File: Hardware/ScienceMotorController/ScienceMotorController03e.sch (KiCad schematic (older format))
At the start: 16 parts

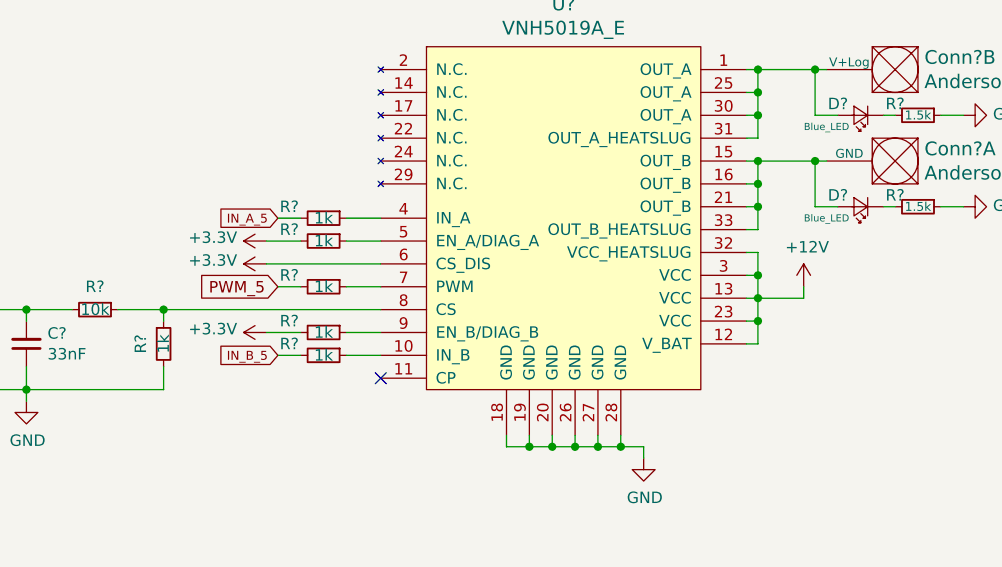
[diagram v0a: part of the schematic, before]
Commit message: changed everything to actuation, added schottky diode, added A/B flags to tiva
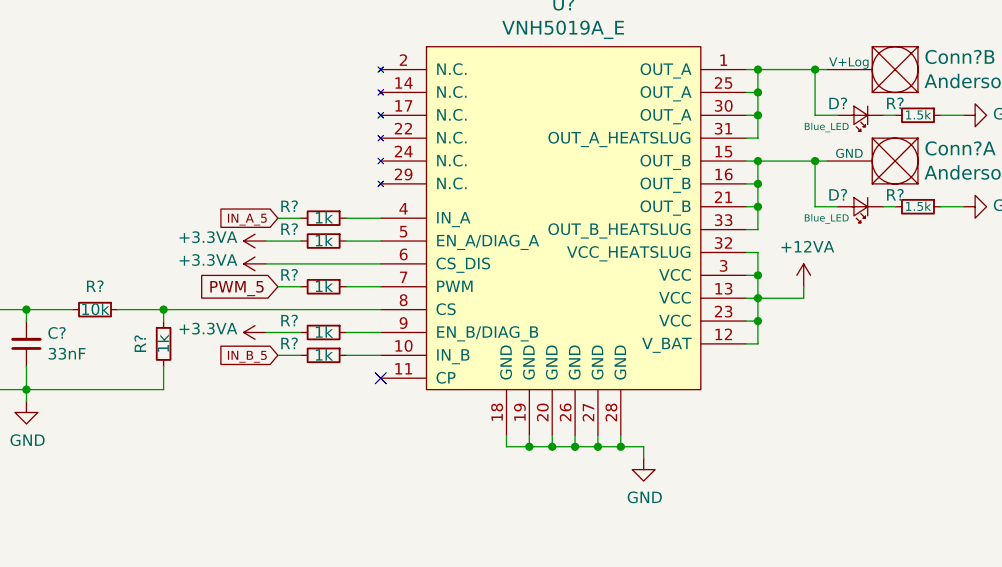
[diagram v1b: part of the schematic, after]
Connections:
- net +12V renamed +12VA
- net +3V3 renamed +3.3VA
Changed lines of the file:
@@
 	6350 4150 6350 4050
 Connection ~ 6350 4050
-$Comp
-L power:+12V #PWR?
-U 1 1 5FAB35E0
-P 6550 3900
-AR Path="/5F7D111E/5FAB35E0" Ref="#PWR?"  Part="1"
-AR Path="/5F7D111E/5FA666AF/5FAB35E0" Ref="#PWR?"  Part="1"
-F 0 "#PWR?" H 6550 3750 50  0001 C CNN
-F 1 "+12V" H 6565 4073 50  0000 C CNN
-F 2 "" H 6550 3900 50  0001 C CNN
-F 3 "" H 6550 3900 50  0001 C CNN
-	1    6550 3900
-	1    0    0    -1
-$EndComp
 Wire Wire Line
 	6550 3900 6550 3950
@@
 Wire Wire Line
 	4350 4100 4200 4100
-$Comp
-L power:+3.3V #PWR?
-U 1 1 5FAB3621
-P 4200 4100
-AR Path="/5F7D111E/5FAB3621" Ref="#PWR?"  Part="1"
-AR Path="/5F7D111E/5FA666AF/5FAB3621" Ref="#PWR?"  Part="1"
-F 0 "#PWR?" H 4200 3950 50  0001 C CNN
-F 1 "+3.3V" V 4215 4228 50  0000 L CNN
-F 2 "" H 4200 4100 50  0001 C CNN
-F 3 "" H 4200 4100 50  0001 C CNN
-	1    4200 4100
-	0    -1   -1   0
-$EndComp
-$Comp
-L power:+3.3V #PWR?
-U 1 1 5FAB3627
-P 4200 3800
-AR Path="/5F7D111E/5FAB3627" Ref="#PWR?"  Part="1"
-AR Path="/5F7D111E/5FA666AF/5FAB3627" Ref="#PWR?"  Part="1"
-F 0 "#PWR?" H 4200 3650 50  0001 C CNN
-F 1 "+3.3V" V 4215 3928 50  0000 L CNN
-F 2 "" H 4200 3800 50  0001 C CNN
-F 3 "" H 4200 3800 50  0001 C CNN
-	1    4200 3800
-	0    -1   -1   0
-$EndComp
 Wire Wire Line
 	4700 3800 4200 3800
@@
 Wire Wire Line
 	4700 3700 4550 3700
-$Comp
-L power:+3.3V #PWR?
-U 1 1 5FAB3635
-P 4200 3700
-AR Path="/5F7D111E/5FAB3635" Ref="#PWR?"  Part="1"
-AR Path="/5F7D111E/5FA666AF/5FAB3635" Ref="#PWR?"  Part="1"
-F 0 "#PWR?" H 4200 3550 50  0001 C CNN
-F 1 "+3.3V" V 4215 3828 50  0000 L CNN
-F 2 "" H 4200 3700 50  0001 C CNN
-F 3 "" H 4200 3700 50  0001 C CNN
-	1    4200 3700
-	0    -1   -1   0
-$EndComp
 Wire Wire Line
 	4350 3700 4200 3700
@@
 Text Notes 7200 6950 0    197  ~ 0
 Sheet 03e: Motor Driver 5
+$Comp
+L power:+3.3VA #PWR?
+U 1 1 5F8264AF
+P 4200 3700
+F 0 "#PWR?" H 4200 3550 50  0001 C CNN
+F 1 "+3.3VA" V 4215 3827 50  0000 L CNN
+F 2 "" H 4200 3700 50  0001 C CNN
+F 3 "" H 4200 3700 50  0001 C CNN
+	1    4200 3700
+	0    -1   -1   0
+$EndComp
+$Comp
+L power:+3.3VA #PWR?
+U 1 1 5F827713
+P 4200 3800
+F 0 "#PWR?" H 4200 3650 50  0001 C CNN
+F 1 "+3.3VA" V 4215 3927 50  0000 L CNN
+F 2 "" H 4200 3800 50  0001 C CNN
+F 3 "" H 4200 3800 50  0001 C CNN
+	1    4200 3800
+	0    -1   -1   0
+$EndComp
+$Comp
+L power:+3.3VA #PWR?
+U 1 1 5F8278A2
+P 4200 4100
+F 0 "#PWR?" H 4200 3950 50  0001 C CNN
+F 1 "+3.3VA" V 4215 4227 50  0000 L CNN
+F 2 "" H 4200 4100 50  0001 C CNN
+F 3 "" H 4200 4100 50  0001 C CNN
+	1    4200 4100
+	0    -1   -1   0
+$EndComp
+$Comp
+L power:+12VA #PWR?
+U 1 1 5F8282D6
+P 6550 3900
+F 0 "#PWR?" H 6550 3750 50  0001 C CNN
+F 1 "+12VA" H 6565 4073 50  0000 C CNN
+F 2 "" H 6550 3900 50  0001 C CNN
+F 3 "" H 6550 3900 50  0001 C CNN
+	1    6550 3900
+	1    0    0    -1
+$EndComp
 $EndSCHEMATC

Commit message: fixed hierarchical
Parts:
- added FB? (x2): Ferrite_Bead, symbol Device:Ferrite_Bead_Small
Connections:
- net at U?.1 (OUT_A), U?.25 (OUT_A), U?.30 (OUT_A)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: now also FB?.2; no longer Conn?.2 (V+Log), D?.2 (A)
- net at U?.15 (OUT_B), U?.16 (OUT_B), U?.21 (OUT_B)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: now also FB?.2; no longer Conn?.1 (GND), D?.2 (A)
- net IN_A_5 renamed In_A_5
- net IN_B_5 renamed In_B_5
- new net: Conn?.2 (V+Log), D?.2 (A), FB?.1
- new net: Conn?.1 (GND), D?.2 (A), FB?.1
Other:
- moved on the sheet: Conn?A, Conn?B, D?, R?

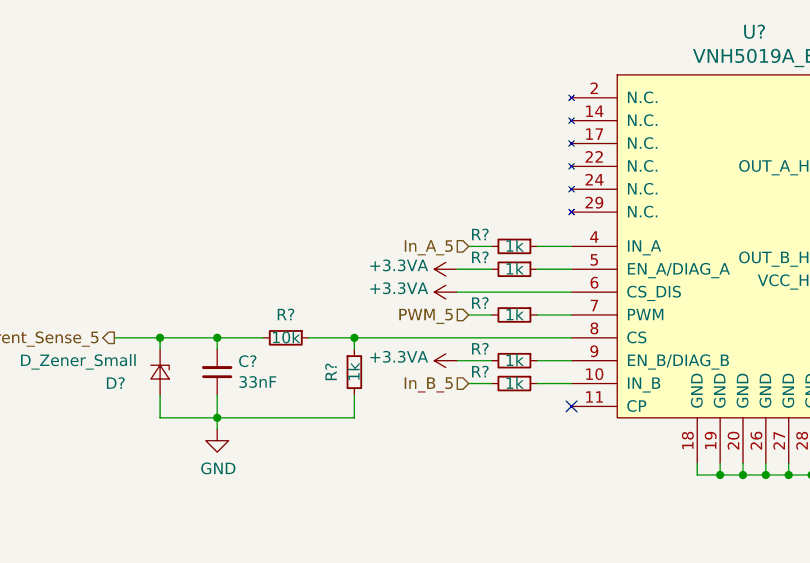
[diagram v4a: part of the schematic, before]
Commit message: Fixed 3.3V, added encoders
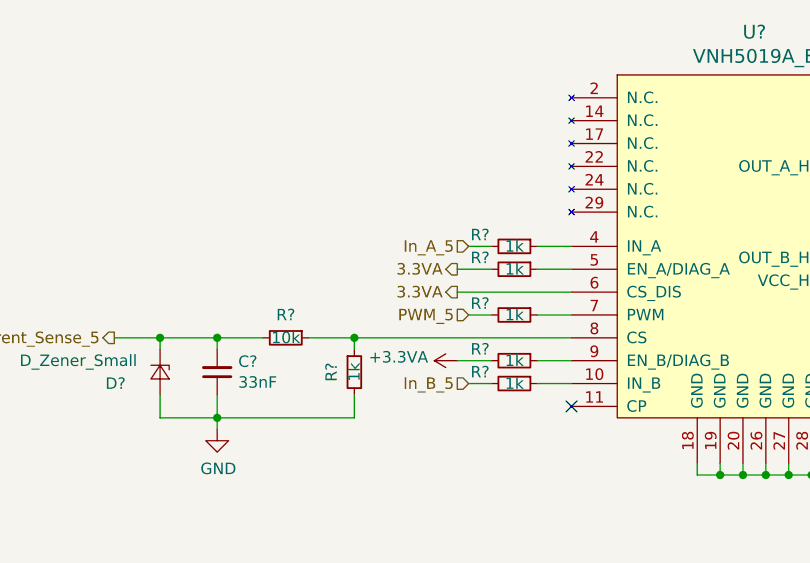
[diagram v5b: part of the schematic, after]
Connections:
- net +3.3VA: no longer R?.2, U?.6 (CS_DIS)
- new net 3.3VA: R?.2, U?.6 (CS_DIS)
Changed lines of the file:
@@
 $Descr A4 11693 8268
 encoding utf-8
-Sheet 7 10
+Sheet 7 11
 Title ""
 Date ""
@@
 $Comp
 L power:+3.3VA #PWR?
-U 1 1 5F8264AF
-P 4200 3700
-AR Path="/5F7D111E/5FA666AF/5F8264AF" Ref="#PWR?"  Part="1"
-AR Path="/5F9082FE/5F8264AF" Ref="#PWR?"  Part="1"
-AR Path="/5F7148FA/5FA34ADB/5F8264AF" Ref="#PWR?"  Part="1"
-F 0 "#PWR?" H 4200 3550 50  0001 C CNN
-F 1 "+3.3VA" V 4215 3827 50  0000 L CNN
-F 2 "" H 4200 3700 50  0001 C CNN
-F 3 "" H 4200 3700 50  0001 C CNN
-	1    4200 3700
-	0    -1   -1   0
-$EndComp
-$Comp
-L power:+3.3VA #PWR?
-U 1 1 5F827713
-P 4200 3800
-AR Path="/5F7D111E/5FA666AF/5F827713" Ref="#PWR?"  Part="1"
-AR Path="/5F9082FE/5F827713" Ref="#PWR?"  Part="1"
-AR Path="/5F7148FA/5FA34ADB/5F827713" Ref="#PWR?"  Part="1"
-F 0 "#PWR?" H 4200 3650 50  0001 C CNN
-F 1 "+3.3VA" V 4215 3927 50  0000 L CNN
-F 2 "" H 4200 3800 50  0001 C CNN
-F 3 "" H 4200 3800 50  0001 C CNN
-	1    4200 3800
-	0    -1   -1   0
-$EndComp
-$Comp
-L power:+3.3VA #PWR?
 U 1 1 5F8278A2
 P 4200 4100
@@
 Text HLabel 2700 4000 0    50   Output ~ 0
 Current_Sense_5
+Text HLabel 4200 3700 0    50   Output ~ 0
+3.3VA
+Text HLabel 4200 3800 0    50   Output ~ 0
+3.3VA
 $EndSCHEMATC

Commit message: added logic line
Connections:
- net 3.3VA is gone; now on net 3.3V: R?.2, U?.6 (CS_DIS)
- net +3.3VA renamed 3.3V
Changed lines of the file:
@@
 Sheet 03e: Motor Driver 5
-$Comp
-L power:+3.3VA #PWR?
-U 1 1 5F8278A2
-P 4200 4100
-AR Path="/5F7D111E/5FA666AF/5F8278A2" Ref="#PWR?"  Part="1"
-AR Path="/5F9082FE/5F8278A2" Ref="#PWR?"  Part="1"
-AR Path="/5F7148FA/5FA34ADB/5F8278A2" Ref="#PWR?"  Part="1"
-F 0 "#PWR?" H 4200 3950 50  0001 C CNN
-F 1 "+3.3VA" V 4215 4227 50  0000 L CNN
-F 2 "" H 4200 4100 50  0001 C CNN
-F 3 "" H 4200 4100 50  0001 C CNN
-	1    4200 4100
-	0    -1   -1   0
-$EndComp
 $Comp
 L power:+12VA #PWR?
@@
 Current_Sense_5
 Text HLabel 4200 3700 0    50   Output ~ 0
-3.3VA
+3.3V
 Text HLabel 4200 3800 0    50   Output ~ 0
-3.3VA
+3.3V
+Text HLabel 4200 4100 0    50   Output ~ 0
+3.3V
 $EndSCHEMATC

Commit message: annotated
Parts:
- C6: renamed from C?; footprint (none) -> Capacitor_SMD:C_0603_1608Metric_Pad1.05x0.95mm_HandSolder
- gave numbers to parts that had none: 16
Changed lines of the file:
@@
 AR Path="/5F7D111E/5FA666AF/5FAB35CE" Ref="U?"  Part="1"
 AR Path="/5F9082FE/5FAB35CE" Ref="U?"  Part="1"
-AR Path="/5F7148FA/5FA34ADB/5FAB35CE" Ref="U?"  Part="1"
-F 0 "U?" H 5500 6037 60  0000 C CNN
+AR Path="/5F7148FA/5FA34ADB/5FAB35CE" Ref="U6"  Part="1"
+F 0 "U6" H 5500 6037 60  0000 C CNN
 F 1 "VNH5019A_E" H 5500 5931 60  0000 C CNN
 F 2 "" H 4900 5650 60  0001 C CNN
@@
 AR Path="/5F7D111E/5FA666AF/5FAB35EB" Ref="R?"  Part="1"
 AR Path="/5F9082FE/5FAB35EB" Ref="R?"  Part="1"
-AR Path="/5F7148FA/5FA34ADB/5FAB35EB" Ref="R?"  Part="1"
-F 0 "R?" V 4400 3750 50  0000 C CNN
+AR Path="/5F7148FA/5FA34ADB/5FAB35EB" Ref="R37"  Part="1"
+F 0 "R37" V 4400 3750 50  0000 C CNN
 F 1 "1k" V 4450 3900 50  0000 C CNN
 F 2 "" H 4450 3900 50  0001 C CNN
@@
 AR Path="/5F7D111E/5FA666AF/5FAB35F1" Ref="R?"  Part="1"
 AR Path="/5F9082FE/5FAB35F1" Ref="R?"  Part="1"
-AR Path="/5F7148FA/5FA34ADB/5FAB35F1" Ref="R?"  Part="1"
-F 0 "R?" V 3650 4150 50  0000 C CNN
+AR Path="/5F7148FA/5FA34ADB/5FAB35F1" Ref="R34"  Part="1"
+F 0 "R34" V 3650 4150 50  0000 C CNN
 F 1 "1k" V 3750 4150 50  0000 C CNN
 F 2 "" H 3750 4150 50  0001 C CNN
@@
 AR Path="/5F7D111E/5FA666AF/5FAB35F7" Ref="C?"  Part="1"
 AR Path="/5F9082FE/5FAB35F7" Ref="C?"  Part="1"
-AR Path="/5F7148FA/5FA34ADB/5FAB35F7" Ref="C?"  Part="1"
-F 0 "C?" H 3058 4104 50  0000 R CNN
+AR Path="/5F7148FA/5FA34ADB/5FAB35F7" Ref="C6"  Part="1"
+F 0 "C6" H 3058 4104 50  0000 R CNN
 F 1 "33nF" H 3058 4195 50  0000 R CNN
-F 2 "" H 3150 4150 50  0001 C CNN
+F 2 "Capacitor_SMD:C_0603_1608Metric_Pad1.05x0.95mm_HandSolder" H 3150 4150 50  0001 C CNN
 F 3 "~" H 3150 4150 50  0001 C CNN
 	1    3150 4150
@@
 AR Path="/5F7D111E/5FA666AF/5FAB35FD" Ref="D?"  Part="1"
 AR Path="/5F9082FE/5FAB35FD" Ref="D?"  Part="1"
-AR Path="/5F7148FA/5FA34ADB/5FAB35FD" Ref="D?"  Part="1"
-F 0 "D?" V 2950 4000 50  0000 R CNN
+AR Path="/5F7148FA/5FA34ADB/5FAB35FD" Ref="D16"  Part="1"
+F 0 "D16" V 2950 4000 50  0000 R CNN
 F 1 "D_Zener_Small" V 2850 4050 50  0000 R CNN
 F 2 "" V 2900 4150 50  0001 C CNN
@@
 AR Path="/5F7D111E/5FA666AF/5FAB3603" Ref="R?"  Part="1"
 AR Path="/5F9082FE/5FAB3603" Ref="R?"  Part="1"
-AR Path="/5F7148FA/5FA34ADB/5FAB3603" Ref="R?"  Part="1"
-F 0 "R?" V 3350 4000 50  0000 C CNN
+AR Path="/5F7148FA/5FA34ADB/5FAB3603" Ref="R33"  Part="1"
+F 0 "R33" V 3350 4000 50  0000 C CNN
 F 1 "10k" V 3450 4000 50  0000 C CNN
 F 2 "" H 3450 4000 50  0001 C CNN
@@
 AR Path="/5F7D111E/5FA666AF/5FAB3619" Ref="R?"  Part="1"
 AR Path="/5F9082FE/5FAB3619" Ref="R?"  Part="1"
-AR Path="/5F7148FA/5FA34ADB/5FAB3619" Ref="R?"  Part="1"
-F 0 "R?" V 4400 3950 50  0000 C CNN
+AR Path="/5F7148FA/5FA34ADB/5FAB3619" Ref="R38"  Part="1"
+F 0 "R38" V 4400 3950 50  0000 C CNN
 F 1 "1k" V 4450 4100 50  0000 C CNN
 F 2 "" H 4450 4100 50  0001 C CNN
@@
 AR Path="/5F7D111E/5FA666AF/5FAB362E" Ref="R?"  Part="1"
 AR Path="/5F9082FE/5FAB362E" Ref="R?"  Part="1"
-AR Path="/5F7148FA/5FA34ADB/5FAB362E" Ref="R?"  Part="1"
-F 0 "R?" V 4400 3550 50  0000 C CNN
+AR Path="/5F7148FA/5FA34ADB/5FAB362E" Ref="R36"  Part="1"
+F 0 "R36" V 4400 3550 50  0000 C CNN
 F 1 "1k" V 4450 3700 50  0000 C CNN
 F 2 "" H 4450 3700 50  0001 C CNN
@@
 AR Path="/5F7D111E/5FA666AF/5FAB363C" Ref="R?"  Part="1"
 AR Path="/5F9082FE/5FAB363C" Ref="R?"  Part="1"
-AR Path="/5F7148FA/5FA34ADB/5FAB363C" Ref="R?"  Part="1"
-F 0 "R?" V 4400 3450 50  0000 C CNN
+AR Path="/5F7148FA/5FA34ADB/5FAB363C" Ref="R35"  Part="1"
+F 0 "R35" V 4400 3450 50  0000 C CNN
 F 1 "1k" V 4450 3600 50  0000 C CNN
 F 2 "" H 4450 3600 50  0001 C CNN
@@
 AR Path="/5F7D111E/5FA666AF/5FAB3646" Ref="R?"  Part="1"
 AR Path="/5F9082FE/5FAB3646" Ref="R?"  Part="1"
-AR Path="/5F7148FA/5FA34ADB/5FAB3646" Ref="R?"  Part="1"
-F 0 "R?" V 4400 4050 50  0000 C CNN
+AR Path="/5F7148FA/5FA34ADB/5FAB3646" Ref="R39"  Part="1"
+F 0 "R39" V 4400 4050 50  0000 C CNN
 F 1 "1k" V 4450 4200 50  0000 C CNN
 F 2 "" H 4450 4200 50  0001 C CNN
@@
 AR Path="/5F7D111E/5FA666AF/5FAB365E" Ref="#PWR?"  Part="1"
 AR Path="/5F9082FE/5FAB365E" Ref="#PWR?"  Part="1"
-AR Path="/5F7148FA/5FA34ADB/5FAB365E" Ref="#PWR?"  Part="1"
-F 0 "#PWR?" H 5850 4400 50  0001 C CNN
+AR Path="/5F7148FA/5FA34ADB/5FAB365E" Ref="#PWR032"  Part="1"
+F 0 "#PWR032" H 5850 4400 50  0001 C CNN
 F 1 "GND" H 5855 4477 50  0000 C CNN
 F 2 "" H 5850 4650 50  0001 C CNN
@@
 AR Path="/5F7D111E/5FA666AF/5FAB3668" Ref="#PWR?"  Part="1"
 AR Path="/5F9082FE/5FAB3668" Ref="#PWR?"  Part="1"
-AR Path="/5F7148FA/5FA34ADB/5FAB3668" Ref="#PWR?"  Part="1"
-F 0 "#PWR?" H 3150 4150 50  0001 C CNN
+AR Path="/5F7148FA/5FA34ADB/5FAB3668" Ref="#PWR031"  Part="1"
+F 0 "#PWR031" H 3150 4150 50  0001 C CNN
 F 1 "GND" H 3155 4227 50  0000 C CNN
 F 2 "" H 3150 4400 50  0001 C CNN
@@
 AR Path="/5F7D111E/5FA666AF/5FAB3680" Ref="Conn?"  Part="1"
 AR Path="/5F9082FE/5FAB3680" Ref="Conn?"  Part="1"
-AR Path="/5F7148FA/5FA34ADB/5FAB3680" Ref="Conn?"  Part="1"
-F 0 "Conn?" H 7472 3297 60  0000 R CNN
+AR Path="/5F7148FA/5FA34ADB/5FAB3680" Ref="Conn5"  Part="1"
+F 0 "Conn5" H 7472 3297 60  0000 R CNN
 F 1 "AndersonPP" H 7472 3403 60  0000 R CNN
 F 2 "" H 7350 2700 60  0001 C CNN
@@
 AR Path="/5F7D111E/5FA666AF/5FAB3686" Ref="Conn?"  Part="2"
 AR Path="/5F9082FE/5FAB3686" Ref="Conn?"  Part="2"
-AR Path="/5F7148FA/5FA34ADB/5FAB3686" Ref="Conn?"  Part="2"
-F 0 "Conn?" H 7472 2897 60  0000 R CNN
+AR Path="/5F7148FA/5FA34ADB/5FAB3686" Ref="Conn5"  Part="2"
+F 0 "Conn5" H 7472 2897 60  0000 R CNN
 F 1 "AndersonPP" H 7472 3003 60  0000 R CNN
 F 2 "" H 7350 2300 60  0001 C CNN
@@
 AR Path="/5F7D111E/5FA666AF/5FAB369A" Ref="D?"  Part="1"
 AR Path="/5F9082FE/5FAB369A" Ref="D?"  Part="1"
-AR Path="/5F7148FA/5FA34ADB/5FAB369A" Ref="D?"  Part="1"
-F 0 "D?" H 7350 3100 50  0000 C CNN
+AR Path="/5F7148FA/5FA34ADB/5FAB369A" Ref="D17"  Part="1"
+F 0 "D17" H 7350 3100 50  0000 C CNN
 F 1 "Blue_LED" H 7400 3200 31  0000 C CNN
 F 2 "" V 7250 3150 50  0001 C CNN
@@
 AR Path="/5F7D111E/5FA666AF/5FAB36A0" Ref="D?"  Part="1"
 AR Path="/5F9082FE/5FAB36A0" Ref="D?"  Part="1"
-AR Path="/5F7148FA/5FA34ADB/5FAB36A0" Ref="D?"  Part="1"
-F 0 "D?" H 7350 3500 50  0000 C CNN
+AR Path="/5F7148FA/5FA34ADB/5FAB36A0" Ref="D18"  Part="1"
+F 0 "D18" H 7350 3500 50  0000 C CNN
 F 1 "Blue_LED" H 7400 3600 31  0000 C CNN
 F 2 "" V 7250 3550 50  0001 C CNN
@@
 AR Path="/5F7D111E/5FA666AF/5FAB36A6" Ref="R?"  Part="1"
 AR Path="/5F9082FE/5FAB36A6" Ref="R?"  Part="1"
-AR Path="/5F7148FA/5FA34ADB/5FAB36A6" Ref="R?"  Part="1"
-F 0 "R?" V 7450 3450 50  0000 C CNN
+AR Path="/5F7148FA/5FA34ADB/5FAB36A6" Ref="R41"  Part="1"
+F 0 "R41" V 7450 3450 50  0000 C CNN
 F 1 "1.5k" V 7500 3550 39  0000 C CNN
 F 2 "" H 7500 3550 50  0001 C CNN
@@
 AR Path="/5F7D111E/5FA666AF/5FAB36AC" Ref="R?"  Part="1"
 AR Path="/5F9082FE/5FAB36AC" Ref="R?"  Part="1"
-AR Path="/5F7148FA/5FA34ADB/5FAB36AC" Ref="R?"  Part="1"
-F 0 "R?" V 7450 3050 50  0000 C CNN
+AR Path="/5F7148FA/5FA34ADB/5FAB36AC" Ref="R40"  Part="1"
+F 0 "R40" V 7450 3050 50  0000 C CNN
 F 1 "1.5k" V 7500 3150 39  0000 C CNN
 F 2 "" H 7500 3150 50  0001 C CNN
@@
 AR Path="/5F7D111E/5FA666AF/5FAB36B4" Ref="#PWR?"  Part="1"
 AR Path="/5F9082FE/5FAB36B4" Ref="#PWR?"  Part="1"
-AR Path="/5F7148FA/5FA34ADB/5FAB36B4" Ref="#PWR?"  Part="1"
-F 0 "#PWR?" H 7700 2900 50  0001 C CNN
+AR Path="/5F7148FA/5FA34ADB/5FAB36B4" Ref="#PWR034"  Part="1"
+F 0 "#PWR034" H 7700 2900 50  0001 C CNN
 F 1 "GND" V 7705 3022 50  0000 R CNN
 F 2 "" H 7700 3150 50  0001 C CNN
@@
 AR Path="/5F7D111E/5FA666AF/5FAB36BA" Ref="#PWR?"  Part="1"
 AR Path="/5F9082FE/5FAB36BA" Ref="#PWR?"  Part="1"
-AR Path="/5F7148FA/5FA34ADB/5FAB36BA" Ref="#PWR?"  Part="1"
-F 0 "#PWR?" H 7700 3300 50  0001 C CNN
+AR Path="/5F7148FA/5FA34ADB/5FAB36BA" Ref="#PWR035"  Part="1"
+F 0 "#PWR035" H 7700 3300 50  0001 C CNN
 F 1 "GND" V 7705 3422 50  0000 R CNN
 F 2 "" H 7700 3550 50  0001 C CNN
@@
 AR Path="/5F7D111E/5FA666AF/5F8282D6" Ref="#PWR?"  Part="1"
 AR Path="/5F9082FE/5F8282D6" Ref="#PWR?"  Part="1"
-AR Path="/5F7148FA/5FA34ADB/5F8282D6" Ref="#PWR?"  Part="1"
-F 0 "#PWR?" H 6550 3750 50  0001 C CNN
+AR Path="/5F7148FA/5FA34ADB/5F8282D6" Ref="#PWR033"  Part="1"
+F 0 "#PWR033" H 6550 3750 50  0001 C CNN
 F 1 "+12VA" H 6565 4073 50  0000 C CNN
 F 2 "" H 6550 3900 50  0001 C CNN
@@
 P 6700 2950
 AR Path="/5F9082FE/5F9F76C5" Ref="FB?"  Part="1"
-AR Path="/5F7148FA/5FA34ADB/5F9F76C5" Ref="FB?"  Part="1"
-F 0 "FB?" V 6463 2950 50  0000 C CNN
+AR Path="/5F7148FA/5FA34ADB/5F9F76C5" Ref="FB7"  Part="1"
+F 0 "FB7" V 6463 2950 50  0000 C CNN
 F 1 "Ferrite_Bead" V 6554 2950 50  0000 C CNN
 F 2 "" V 6630 2950 50  0001 C CNN
@@
 P 6700 3350
 AR Path="/5F9082FE/5F9F8032" Ref="FB?"  Part="1"
-AR Path="/5F7148FA/5FA34ADB/5F9F8032" Ref="FB?"  Part="1"
-F 0 "FB?" V 6500 3350 50  0000 C CNN
+AR Path="/5F7148FA/5FA34ADB/5F9F8032" Ref="FB8"  Part="1"
+F 0 "FB8" V 6500 3350 50  0000 C CNN
 F 1 "Ferrite_Bead" V 6600 3450 50  0000 C CNN
 F 2 "" V 6630 3350 50  0001 C CNN
